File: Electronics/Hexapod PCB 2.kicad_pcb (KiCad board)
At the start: 4 copper layers, 53 x 85 mm, 79 parts, among them J1 XT60, J2 leg1, J3 leg2, J4 leg3, J5 leg4, J6 leg5, J7 leg6, J8 USB_C_Receptacle_USB2.0_16P, Q1 IRF4905, Q2 Q_NPN_BCE, Q3 Q_NPN_BCE, SW2 SW_SPST, SW3 SW_SPST, U1 TPS563201, U2 TPS563201, U3 ESP32-S3-WROOM-1, U4 USBLC6-2P6, U5 BNO055, U6 INA226

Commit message: finished the layout of the PCB and fixed all DRC mistakes
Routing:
- net BUS1: track 0.00 -> 79.5 mm, vias 0 -> 2
- net +5V: track 0.00 -> 68.5 mm, vias 0 -> 9
- net I2C_SDA: track 0.00 -> 66.9 mm, vias 0 -> 3
- net I2C_SCL: track 0.00 -> 63.5 mm, vias 0 -> 3
- net VBATT-SENSE: track 0.00 -> 58.4 mm, vias 0 -> 2
- net BUS2: track 0.00 -> 54.1 mm, vias 0 -> 2
- net GND: track 0.00 -> 53.1 mm, vias 0 -> 70
- net STAT_LED: track 0.00 -> 46.3 mm, vias 0 -> 2
- net TX1: track 0.00 -> 43.1 mm, vias 0 -> 2
- net IMU_RESET: track 0.00 -> 37.5 mm, vias 0 -> 2
- net IMU_INT: track 0.00 -> 36.3 mm, vias 0 -> 2
- net +3.3V: track 0.00 -> 30.2 mm, vias 0 -> 15
- net Net-(SW2-A): track 0.00 -> 28.0 mm, vias 0 -> 2
- net TX2: track 0.00 -> 25.3 mm, vias 0 -> 2
- net EN: track 0.00 -> 14.0 mm
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- added copper zone on In2.Cu, net +3.3V
- added copper zone on In2.Cu, net +5V
- added copper zone on B.Cu, net +BATT
- added copper zone on F.Cu, net +BATT
- added copper zone on In1.Cu, net GND
- added copper zone on B.Cu, net SERVO-POWER
- added copper zone on F.Cu, net SERVO-POWER
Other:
- outline, holes or cut-outs redrawn

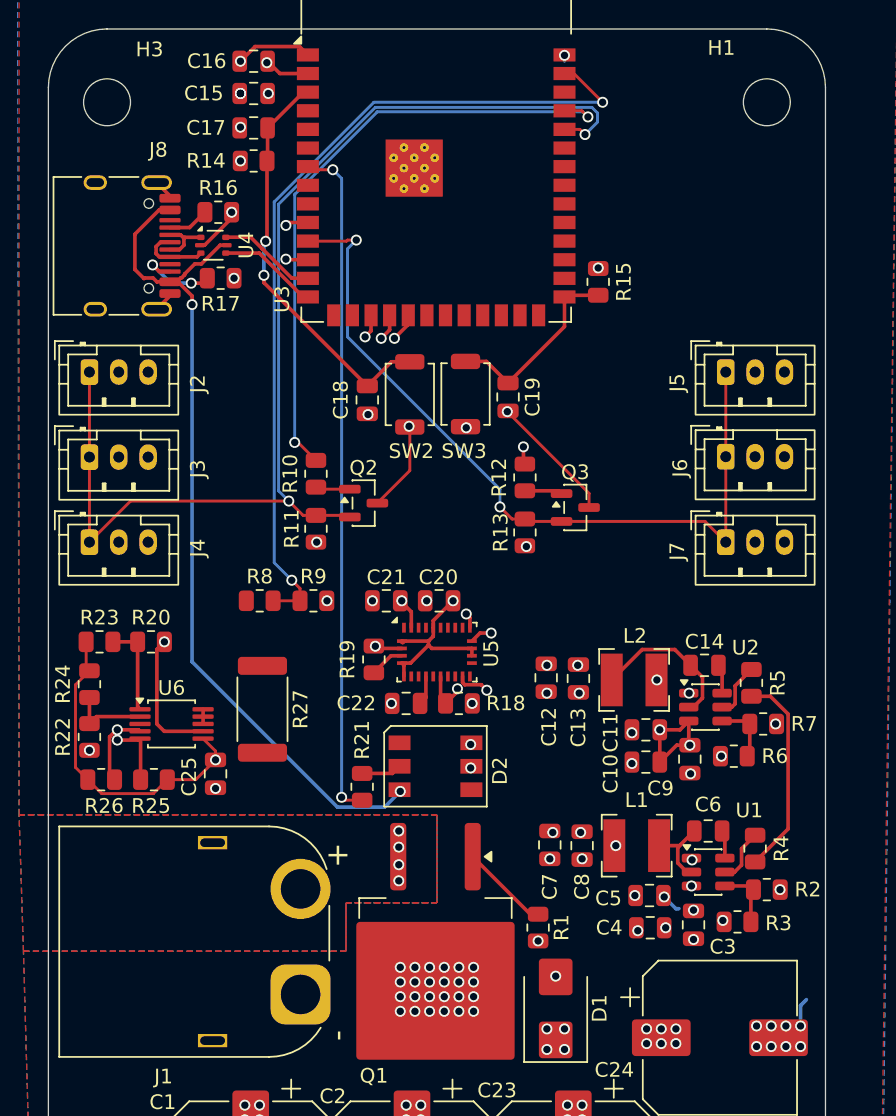
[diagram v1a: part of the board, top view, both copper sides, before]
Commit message: added CAD file into the sctructure of the project and added the PCB STEP file
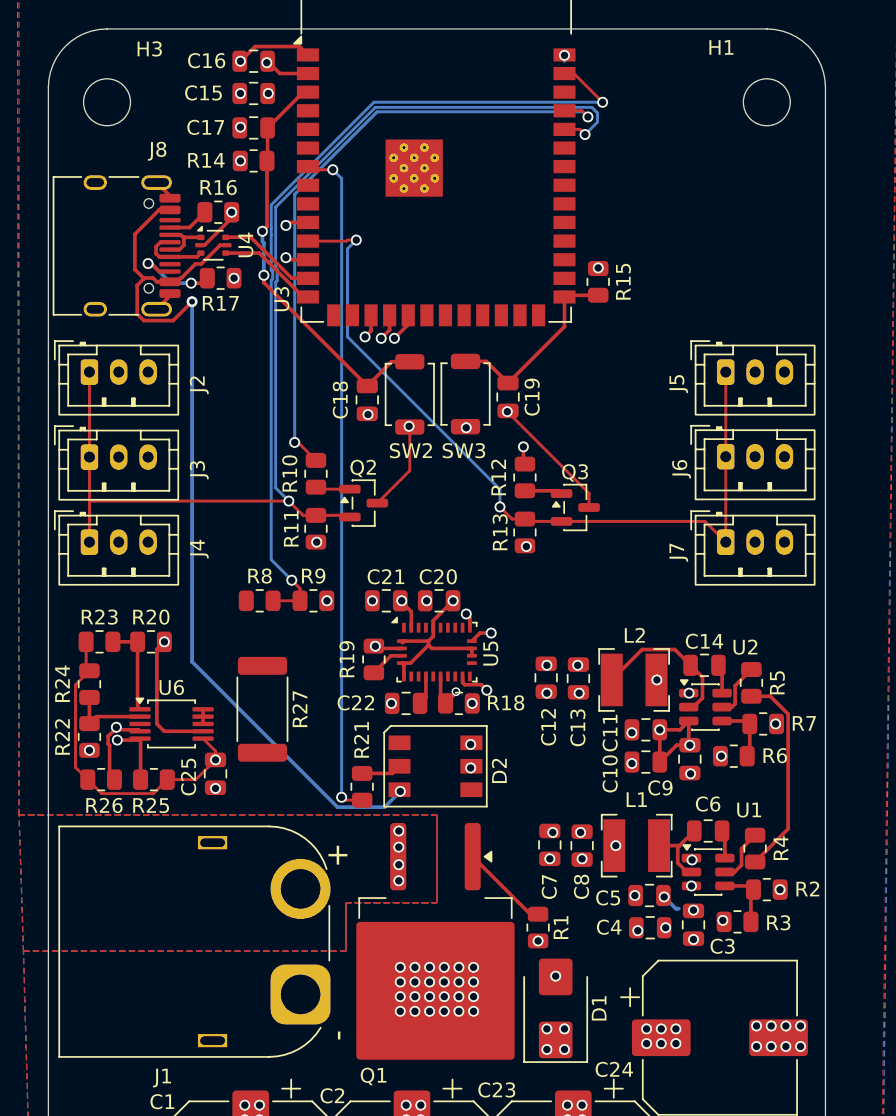
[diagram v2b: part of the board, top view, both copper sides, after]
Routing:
- net +5V: track 68.5 -> 73.2 mm
- net GND: track 53.1 -> 51.1 mm, vias 70 -> 69
- net BUS1: track 79.5 -> 81.4 mm
- net I2C_SDA: track 66.9 -> 67.8 mm
- net Net-(J8-CC2): track 5.76 -> 6.45 mm

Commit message: added some text on the pcb and changed the xt60 from horizontal to vertical mount
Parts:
- added G***: LOGO, LOGO, B.Cu at (164.2, 119.0)
- J1: footprint Connector_AMASS:AMASS_XT60PW-M_1x02_P7.20mm_Horizontal -> Connector_AMASS:AMASS_XT60-M_1x02_P7.20mm_Vertical
- moved J1 67.6 mm to (140.7, 129.2)
- moved C1 61.7 mm to (143.2, 141.2)
- moved C2 61.7 mm to (154.2, 141.2)
- moved C21 61.7 mm to (152.4, 101.8)
- moved C23 61.7 mm to (165.2, 141.2)
- moved C24 61.7 mm to (175.2, 131.6)
- moved C4 61.7 mm to (170.4, 124.1)
- moved J2 61.7 mm to (132.2, 86.2)
- moved J3 61.7 mm to (132.2, 92.0)
- moved J4 61.7 mm to (132.2, 97.8)
- moved R22 61.7 mm to (132.2, 111.1)
- moved R23 61.7 mm to (132.9, 104.6)
- moved R24 61.7 mm to (132.2, 107.5)
- moved C10 61.7 mm to (170.2, 112.8)
- moved C11 61.7 mm to (170.2, 110.6)
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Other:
- board text added: "67"
- board text added: "MadHex"
- board text added: "pcbway"
